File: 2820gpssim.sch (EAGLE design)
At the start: 18 parts, among them IC1 MAX232, IC2 AT90S2313P, IC3 7805, X1 1501_03

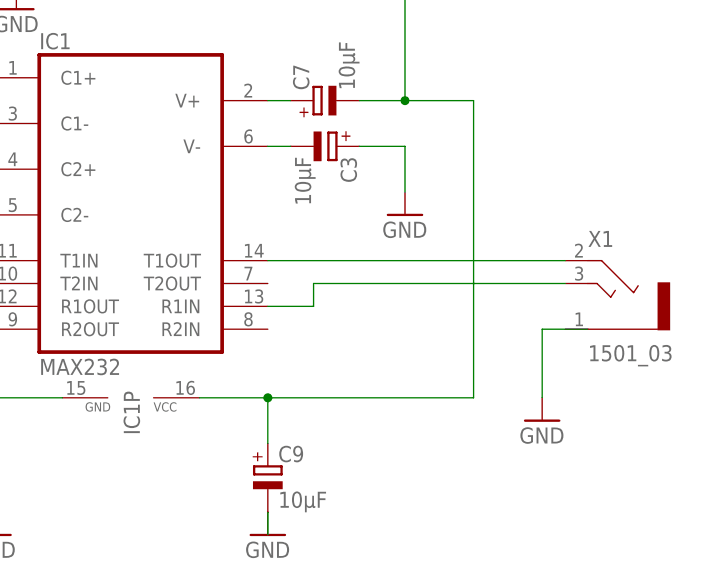
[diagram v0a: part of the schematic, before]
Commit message: Correct schematics
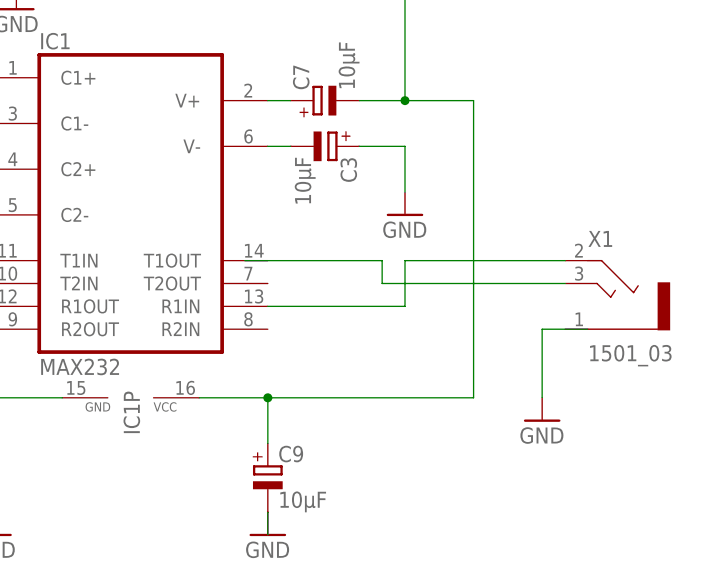
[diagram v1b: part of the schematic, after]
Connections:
- net N$15: no longer IC1G$1.R1IN
- net N$18: now also IC1G$1.R1IN; no longer IC1G$1.T1OUT
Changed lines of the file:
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@@
 <net name="N$15" class="0">
 <segment>
+<wire x1="99.06" y1="12.7" x2="114.3" y2="12.7" width="0.1524" layer="91"/>
+<wire x1="114.3" y1="12.7" x2="114.3" y2="10.16" width="0.1524" layer="91"/>
 <pinref part="X1" gate="G$1" pin="3"/>
-<wire x1="134.62" y1="10.16" x2="106.68" y2="10.16" width="0.1524" layer="91"/>
-<wire x1="106.68" y1="10.16" x2="106.68" y2="7.62" width="0.1524" layer="91"/>
-<pinref part="IC1" gate="G$1" pin="R1IN"/>
-<wire x1="106.68" y1="7.62" x2="101.6" y2="7.62" width="0.1524" layer="91"/>
+<wire x1="114.3" y1="10.16" x2="134.62" y2="10.16" width="0.1524" layer="91"/>
 </segment>
 </net>
 <net name="N$18" class="0">
 <segment>
-<pinref part="IC1" gate="G$1" pin="T1OUT"/>
 <pinref part="X1" gate="G$1" pin="2"/>
-<wire x1="101.6" y1="12.7" x2="134.62" y2="12.7" width="0.1524" layer="91"/>
+<wire x1="134.62" y1="12.7" x2="116.84" y2="12.7" width="0.1524" layer="91"/>
+<wire x1="116.84" y1="12.7" x2="116.84" y2="7.62" width="0.1524" layer="91"/>
+<pinref part="IC1" gate="G$1" pin="R1IN"/>
+<wire x1="116.84" y1="7.62" x2="101.6" y2="7.62" width="0.1524" layer="91"/>
 </segment>
 </net>

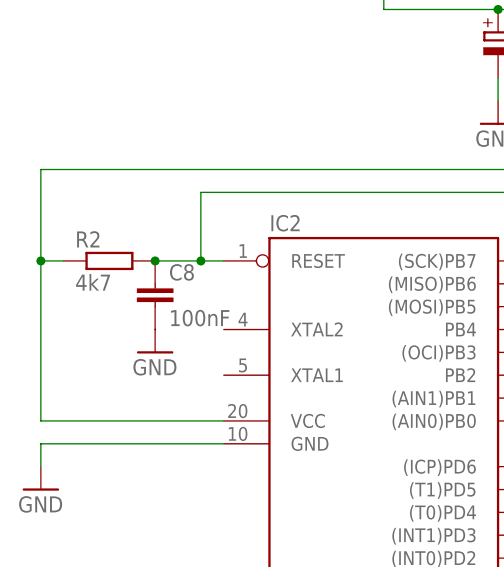
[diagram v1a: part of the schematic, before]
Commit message: Correct RESET resistor
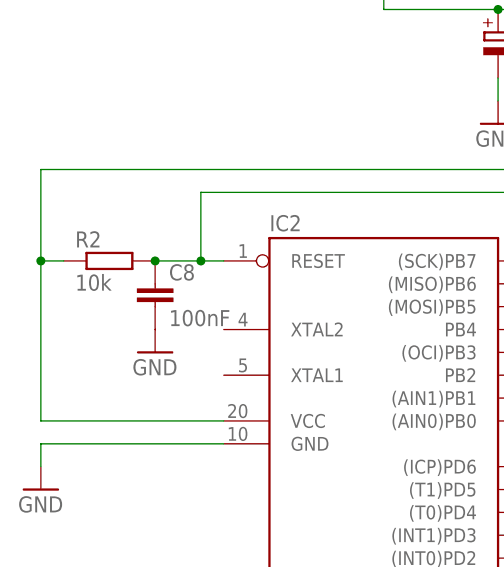
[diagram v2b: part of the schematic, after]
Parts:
- R2: value 4k7 -> 10k
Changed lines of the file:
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@@
 <part name="GND7" library="supply1" deviceset="GND" device=""/>
 <part name="C7" library="resistor" deviceset="CPOL-EU" device="E2.5-5" value="10µF"/>
-<part name="R2" library="rcl" deviceset="R-EU_" device="0204/7" value="4k7"/>
+<part name="R2" library="rcl" deviceset="R-EU_" device="0204/7" value="10k"/>
 <part name="C8" library="resistor" deviceset="C-EU" device="025-025X050" value="100nF"/>
 <part name="GND8" library="supply1" deviceset="GND" device=""/>

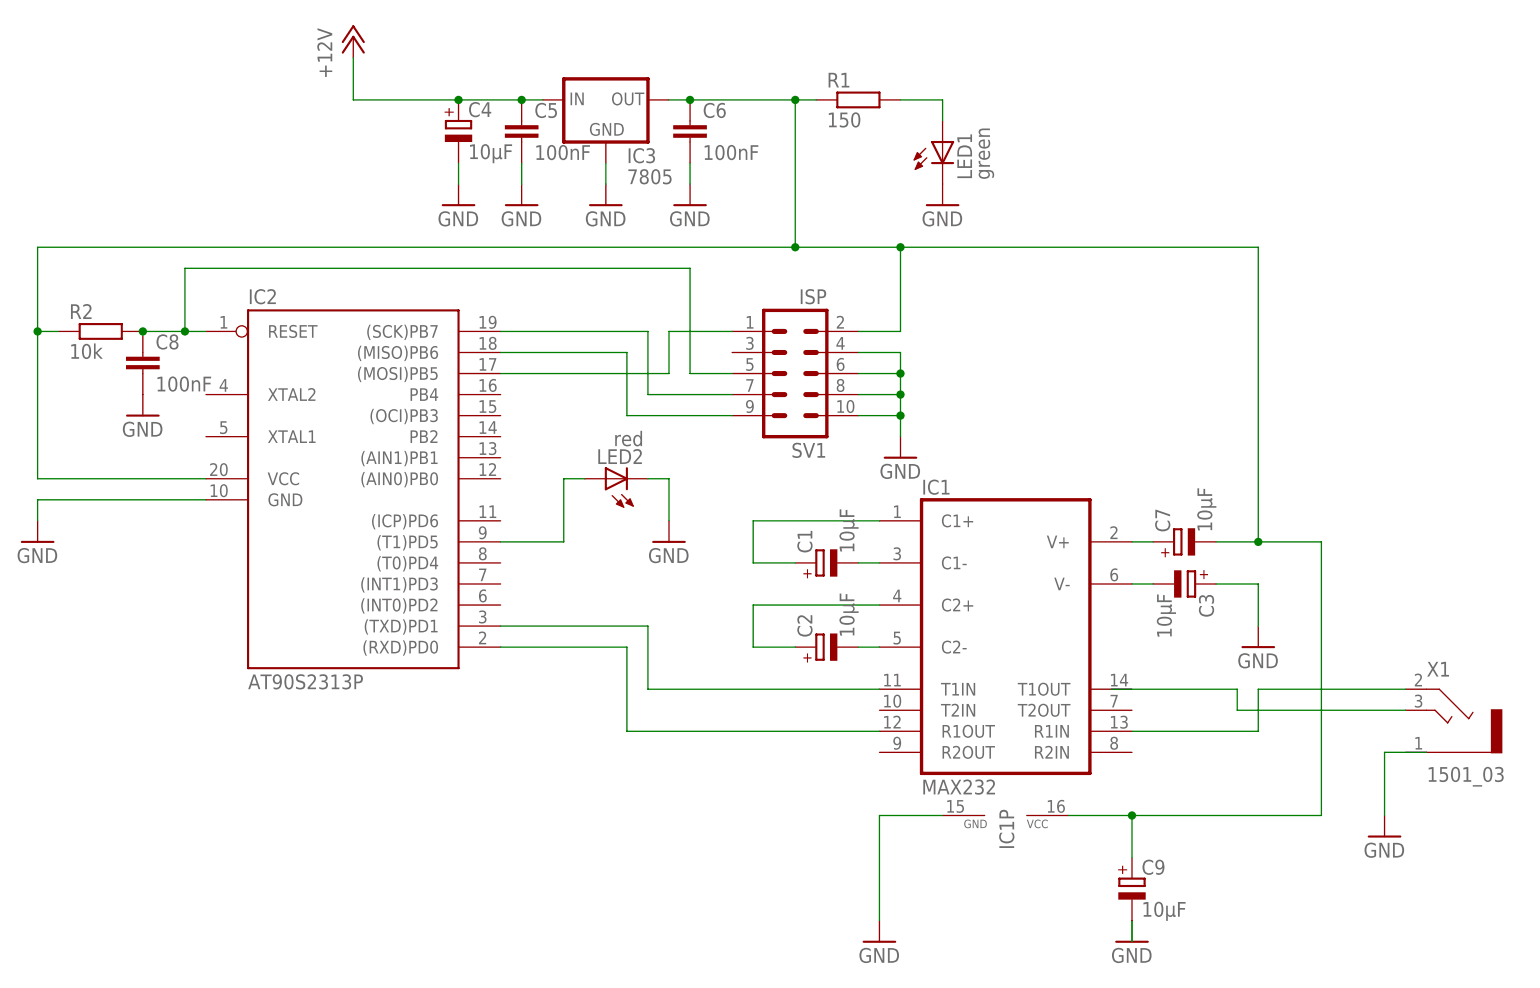
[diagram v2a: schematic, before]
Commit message: Add second ISP connector to schematic
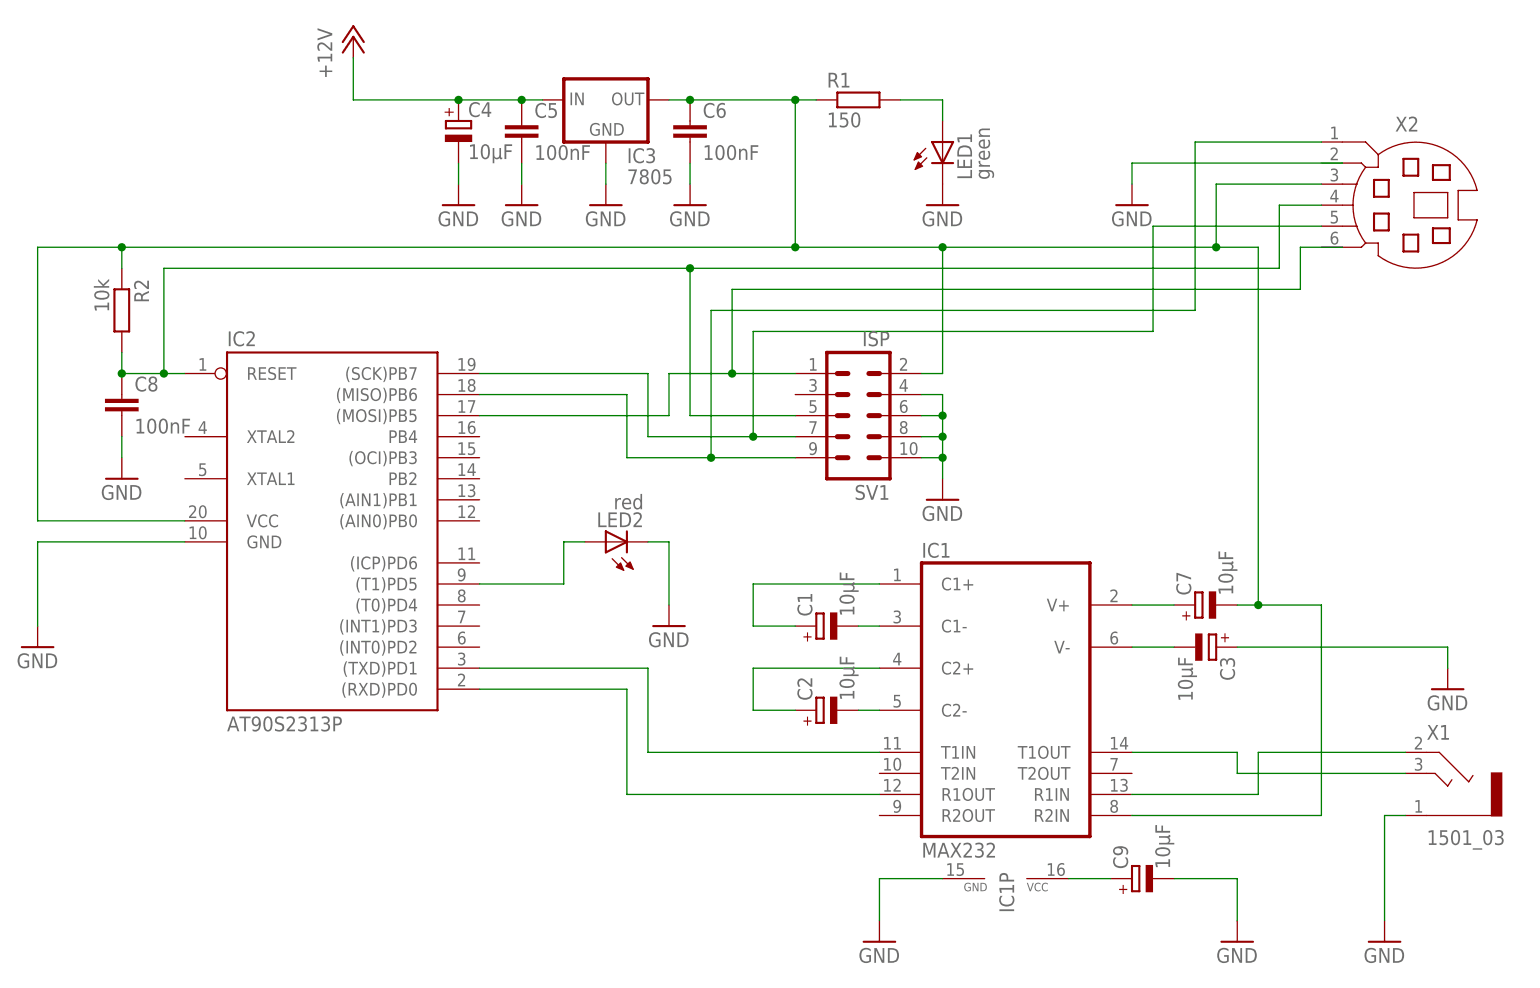
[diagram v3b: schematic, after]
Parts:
- added X2: (no value), con-yamaichi:MD06SS
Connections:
- removed net N$16: IC2.(SCK)PB7, SV1.7
- new net N$14: IC2.(SCK)PB7, SV1.7, X2.5
- net GND: now also C9.-, X1.1
- net N$11: now also X2.4
- net N$12: now also C9.+, IC1P.VCC; no longer C9.-
- net N$15: now also IC1G$1.T1OUT
- net N$17: now also X2.1
- net N$8: now also IC1G$1.R2IN, X2.3; no longer C9.+, IC1P.VCC
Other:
- moved on the sheet: C1, C2, C3, C7, C8, C9, IC1, IC1P, IC2, LED2, R2, SV1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

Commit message: Minor corrections of the schematic
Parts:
- LED2: value red -> yellow
- X2: value (none) -> ISP2
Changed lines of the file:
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@@
 <part name="C8" library="resistor" deviceset="C-EU" device="025-025X050" value="100nF"/>
 <part name="GND8" library="supply1" deviceset="GND" device=""/>
-<part name="LED2" library="led" deviceset="LED" device="3MM" value="red"/>
+<part name="LED2" library="led" deviceset="LED" device="3MM" value="yellow"/>
 <part name="GND9" library="supply1" deviceset="GND" device=""/>
 <part name="SV1" library="con-ml" deviceset="ML10" device="" value="ISP"/>
@@
 <part name="X1" library="con-lumberg" deviceset="1501_03" device=""/>
 <part name="GND13" library="supply1" deviceset="GND" device=""/>
-<part name="X2" library="con-yamaichi" deviceset="MD06SS" device=""/>
+<part name="X2" library="con-yamaichi" deviceset="MD06SS" device="" value="ISP2"/>
 <part name="GND14" library="supply1" deviceset="GND" device=""/>
 </parts>

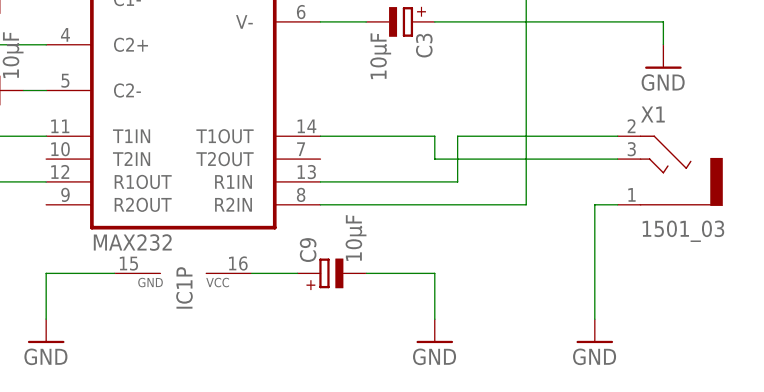
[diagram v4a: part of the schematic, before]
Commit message: Correct error in schematics
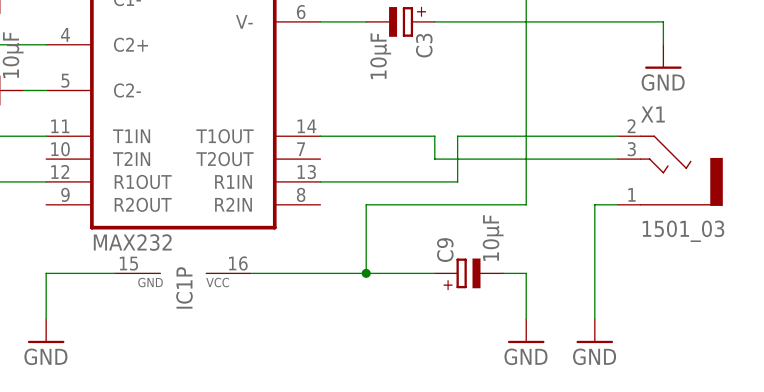
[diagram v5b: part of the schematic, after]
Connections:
- removed net N$12: C9.+, IC1P.VCC
- net N$8: now also C9.+, IC1P.VCC; no longer IC1G$1.R2IN
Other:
- moved on the sheet: C9
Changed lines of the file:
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@@
 <instance part="IC1" gate="P" x="86.36" y="-10.16" rot="R270"/>
 <instance part="GND11" gate="1" x="71.12" y="-17.78"/>
-<instance part="C9" gate="G$1" x="101.6" y="-10.16" rot="R90"/>
-<instance part="GND12" gate="1" x="114.3" y="-17.78"/>
+<instance part="C9" gate="G$1" x="116.84" y="-10.16" rot="R90"/>
+<instance part="GND12" gate="1" x="124.46" y="-17.78"/>
 <instance part="X1" gate="G$1" x="139.7" y="0"/>
 <instance part="GND13" gate="1" x="132.08" y="-17.78"/>
@@
 <pinref part="C9" gate="G$1" pin="-"/>
 <pinref part="GND12" gate="1" pin="GND"/>
-<wire x1="106.68" y1="-10.16" x2="114.3" y2="-10.16" width="0.1524" layer="91"/>
-<wire x1="114.3" y1="-10.16" x2="114.3" y2="-15.24" width="0.1524" layer="91"/>
+<wire x1="121.92" y1="-10.16" x2="124.46" y2="-10.16" width="0.1524" layer="91"/>
+<wire x1="124.46" y1="-10.16" x2="124.46" y2="-15.24" width="0.1524" layer="91"/>
 </segment>
 <segment>
@@
 <wire x1="116.84" y1="22.86" x2="124.46" y2="22.86" width="0.1524" layer="91"/>
 <wire x1="124.46" y1="22.86" x2="124.46" y2="-2.54" width="0.1524" layer="91"/>
-<wire x1="124.46" y1="-2.54" x2="101.6" y2="-2.54" width="0.1524" layer="91"/>
 <junction x="116.84" y="22.86"/>
 <pinref part="X2" gate="G$1" pin="3"/>
@@
 <wire x1="111.76" y1="73.66" x2="111.76" y2="66.04" width="0.1524" layer="91"/>
 <junction x="111.76" y="66.04"/>
-<pinref part="IC1" gate="G$1" pin="R2IN"/>
 <pinref part="R2" gate="G$1" pin="1"/>
 <wire x1="-20.32" y1="63.5" x2="-20.32" y2="66.04" width="0.1524" layer="91"/>
 <junction x="-20.32" y="66.04"/>
+<pinref part="IC1" gate="P" pin="VCC"/>
+<pinref part="C9" gate="G$1" pin="+"/>
+<wire x1="93.98" y1="-10.16" x2="106.68" y2="-10.16" width="0.1524" layer="91"/>
+<wire x1="106.68" y1="-10.16" x2="114.3" y2="-10.16" width="0.1524" layer="91"/>
+<wire x1="124.46" y1="-2.54" x2="106.68" y2="-2.54" width="0.1524" layer="91"/>
+<wire x1="106.68" y1="-2.54" x2="106.68" y2="-10.16" width="0.1524" layer="91"/>
+<junction x="106.68" y="-10.16"/>
 </segment>
 </net>
@@
 </segment>
 </net>
-<net name="N$12" class="0">
-<segment>
-<pinref part="IC1" gate="P" pin="VCC"/>
-<pinref part="C9" gate="G$1" pin="+"/>
-<wire x1="93.98" y1="-10.16" x2="99.06" y2="-10.16" width="0.1524" layer="91"/>
-</segment>
-</net>
